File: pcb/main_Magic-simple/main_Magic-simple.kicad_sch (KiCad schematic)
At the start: 57 parts, among them J1 XT30PW-M, J10 ESC1, J11 ESC2, J12 ESC3, J15 ESC_VM, J2 MPU6050, J4 Encoder1, J5 Encoder2, J9 Sensors, Q1 IRLML2502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

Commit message: pcbAAAAA
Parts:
- removed C10, C9: 10nF, Capacitor_SMD:C_0805_2012Metric, symbol Device:C_Small
- removed C26: 100nF, Capacitor_SMD:C_0805_2012Metric, symbol Device:C_Small
- removed C6: 100nF, Capacitor_SMD:C_0603_1608Metric, symbol Device:C_Small
- removed D2: LED_On, MixLib:LED_0805_2012Metric, symbol Device:LED_Small
- removed D5: WS2812B, LED_SMD:LED_WS2812B_PLCC4_5.0x5.0mm_P3.2mm, symbol LED:WS2812B
- removed J1: XT30PW-M, XT30PW-M:AMASS_XT30PW-M, symbol MixLib:XT30PW-M
- removed J15: ESC_VM, TerminalBlock_Phoenix:TerminalBlock_Phoenix_PT-1,5-6-3.5-H_1x06_P3.50mm_Horizontal, symbol Connector:Screw_Terminal_01x06
- removed J4: Encoder1, Connector_JST:JST_XH_B3B-XH-A_1x03_P2.50mm_Vertical, symbol Connector:Conn_01x03_Pin
- removed J5: Encoder2, Connector_JST:JST_XH_B3B-XH-A_1x03_P2.50mm_Vertical, symbol Connector:Conn_01x03_Pin
- removed JP1: Jumper_2_Small_Open, Resistor_SMD:R_1206_3216Metric, symbol Jumper:Jumper_2_Small_Open
- removed R1: 1k, Resistor_SMD:R_0603_1608Metric, symbol Device:R_Small
- removed R7: 100, Resistor_SMD:R_0805_2012Metric, symbol Device:R_Small
- removed SW3: Boot_SW, MixLib:SW_Slide-03_P2.54_L9_W4_H7, symbol Switch:SW_SPST
- removed U2: ACS712-30A, Package_SO:SOIC-8_3.9x4.9mm_P1.27mm, symbol Sensor_Current:ACS712xLCTR-20A
- removed U3: ACS712-20A, Package_SO:SOIC-8_3.9x4.9mm_P1.27mm, symbol Sensor_Current:ACS712xLCTR-20A
- added C1: 100nF, Capacitor_SMD:C_0805_2012Metric, symbol Device:C_Small
- added D6: LED_BLUE, MixLib:LED_0805_2012Metric, symbol Device:LED_Small
- added F2: 1100mAh, Fuse:Fuse_1812_4532Metric_Pad1.30x3.40mm_HandSolder, symbol Device:Polyfuse
- added J1: PW, Connector_JST:JST_XH_S2B-XH-A_1x02_P2.50mm_Horizontal, symbol Connector:Conn_01x02_Pin
- added J14: UART_Out, Connector_JST:JST_XH_S4B-XH-A_1x04_P2.50mm_Horizontal, symbol Connector:Conn_01x04_Pin
- added J3: LiPo-Battery, TerminalBlock_Phoenix:TerminalBlock_Phoenix_PT-1,5-2-3.5-H_1x02_P3.50mm_Horizontal, symbol Connector:Screw_Terminal_01x02
- added R10: 330, Resistor_SMD:R_0805_2012Metric, symbol Device:R_Small
- added SW3: Boot_Push, Button_Switch_SMD:SW_SPST_CK_RS282G05A3, symbol Switch:SW_Push
- added TP1: Curr1, symbol Connector:TestPoint
- added TP2: Curr2, symbol Connector:TestPoint
- added TP3: Enc1, symbol Connector:TestPoint
- added TP4: Enc2, symbol Connector:TestPoint
- added U6: Mini360, MixLib:Mini360_step-down, symbol MixLib:Mini360
- C11: value 10uF -> 47uF; footprint Capacitor_SMD:C_0805_2012Metric -> Capacitor_SMD:CP_Elec_6.3x5.4
- C28: value 100uF -> 470uF; footprint Capacitor_SMD:CP_Elec_6.3x5.4 -> (none)
- C3: value 1uF -> 22uF
- C5: footprint Capacitor_SMD:C_0603_1608Metric -> Capacitor_SMD:C_0805_2012Metric
- C7: value 100nF -> 1uF
- F1: value 300mA -> 500mA
- R4: value 330 -> 20
- R5: value 100 -> 330
- R6: value 10k -> 1k; footprint Resistor_SMD:R_0805_2012Metric -> Resistor_SMD:R_0603_1608Metric
- R8: value 330 -> 10k
- SW1: footprint MixLib:SW_Slide-03_P2.54_L9_W4_H7 -> (none)
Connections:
- net LEDs is gone; now on net LED_RGB: D3.4 (DIN)
- net +3.3V: now also C5.1, C1.1, F2.2, J1.2 (Pin_2), J14.4 (Pin_4); no longer C11.1, C12.1, C5.2, J9.9 (Pin_9)
- net BOOT: now also SW3.1
- net BUZ: now also R10.1; no longer R8.2
- net CurrESC1&2: now also TP1.1; no longer U1.13 (IO14)
- net CurrESC2: now also TP2.1; no longer U1.12 (IO27)
- net Data_EN: no longer R6.2
- net Enc1: now also TP3.1; no longer U1.11 (IO26)
- net Enc2: now also TP4.1; no longer U1.10 (IO25)
- net GND: now also C5.2, R6.2, R8.1, C1.2, J1.1 (Pin_1), J14.3 (Pin_3), J3.1 (Pin_1), SW3.2, U6.2 (GND); no longer C5.1, R6.1
- net RX: now also J14.1 (Pin_1)
- net TX: now also J14.2 (Pin_2)
- net VM: now also D1.2 (A), J3.2 (Pin_2); no longer SW1.1 (A)
- net Vb: now also SW1.1 (A)
- net at Q1.1 (G): now also R8.2, R10.2; no longer R8.1
- net LED_BLUE: now reaches U1.24 (IO2)
- net LED_BLUE: now also D6.2 (A)
- net LED_RGB: now reaches U1.29 (IO5)
- net at SW1.2 (B): now also U6.1 (IN); no longer D1.2 (A)
- new net: C11.1, C12.1, J9.9 (Pin_9)
- new net: D6.1 (K), R6.1
- new net: F2.1, U6.3 (OUT)
- no-connect marks 5 -> 4
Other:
- removed sheet CH340C
- removed sheet StepDown_CN3903
- note added: "RGB LED"
- note removed: "Bidirectionals"
- note removed: "ESC Current Sensors"
- note removed: "ESP32 connections"
- note removed: "Inputs"
- note removed: "Outputs"
- note removed: "RGB LEDs"
- note removed: "X"
- moved on the sheet: BZ1, C11, C12, C2, C24, C28, D1, D3, H1, H10, H2, H3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

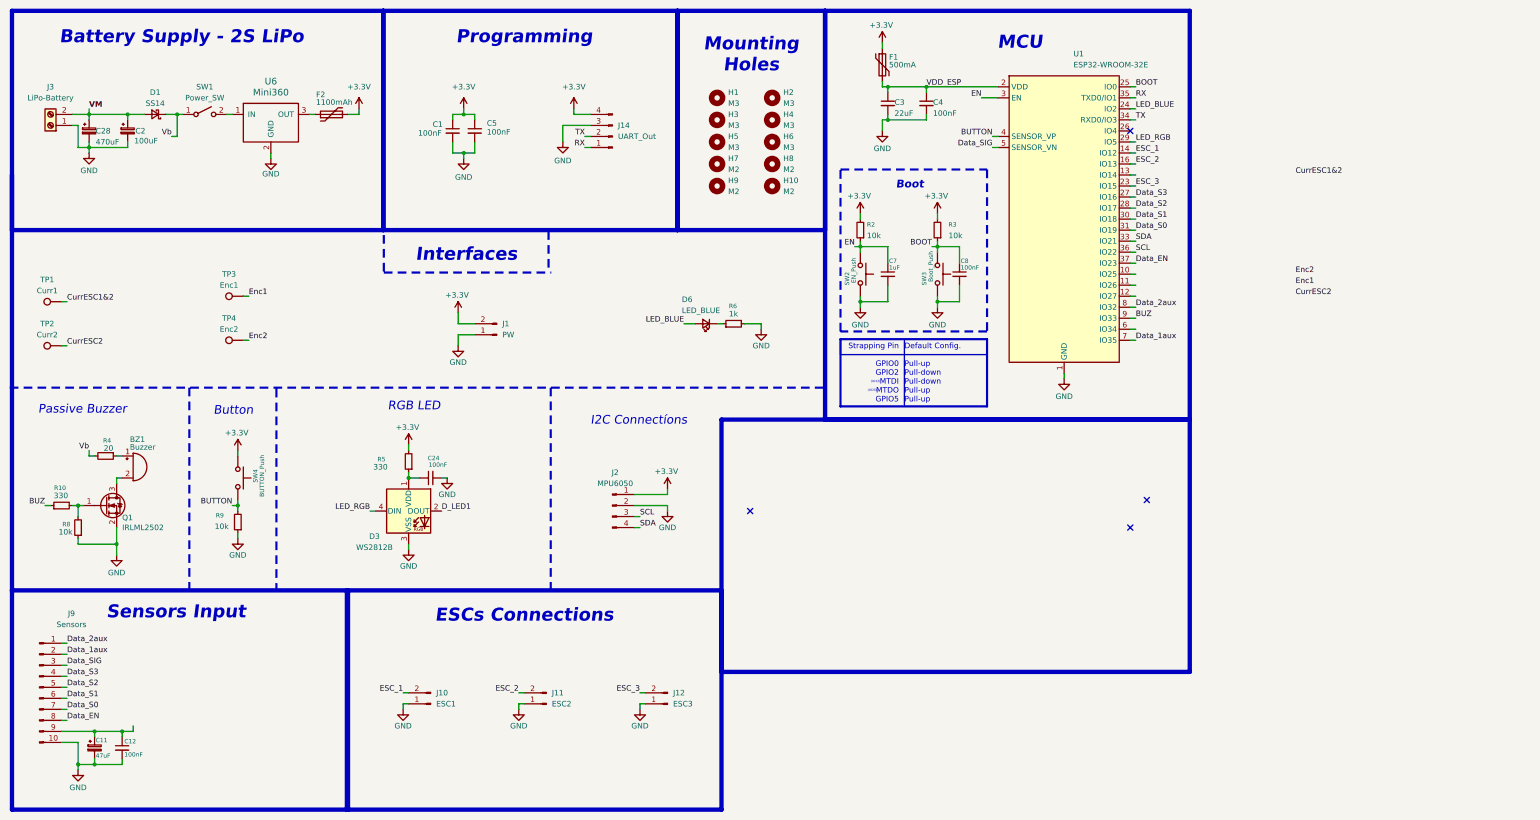
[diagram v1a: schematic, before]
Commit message: simple main board added and donde
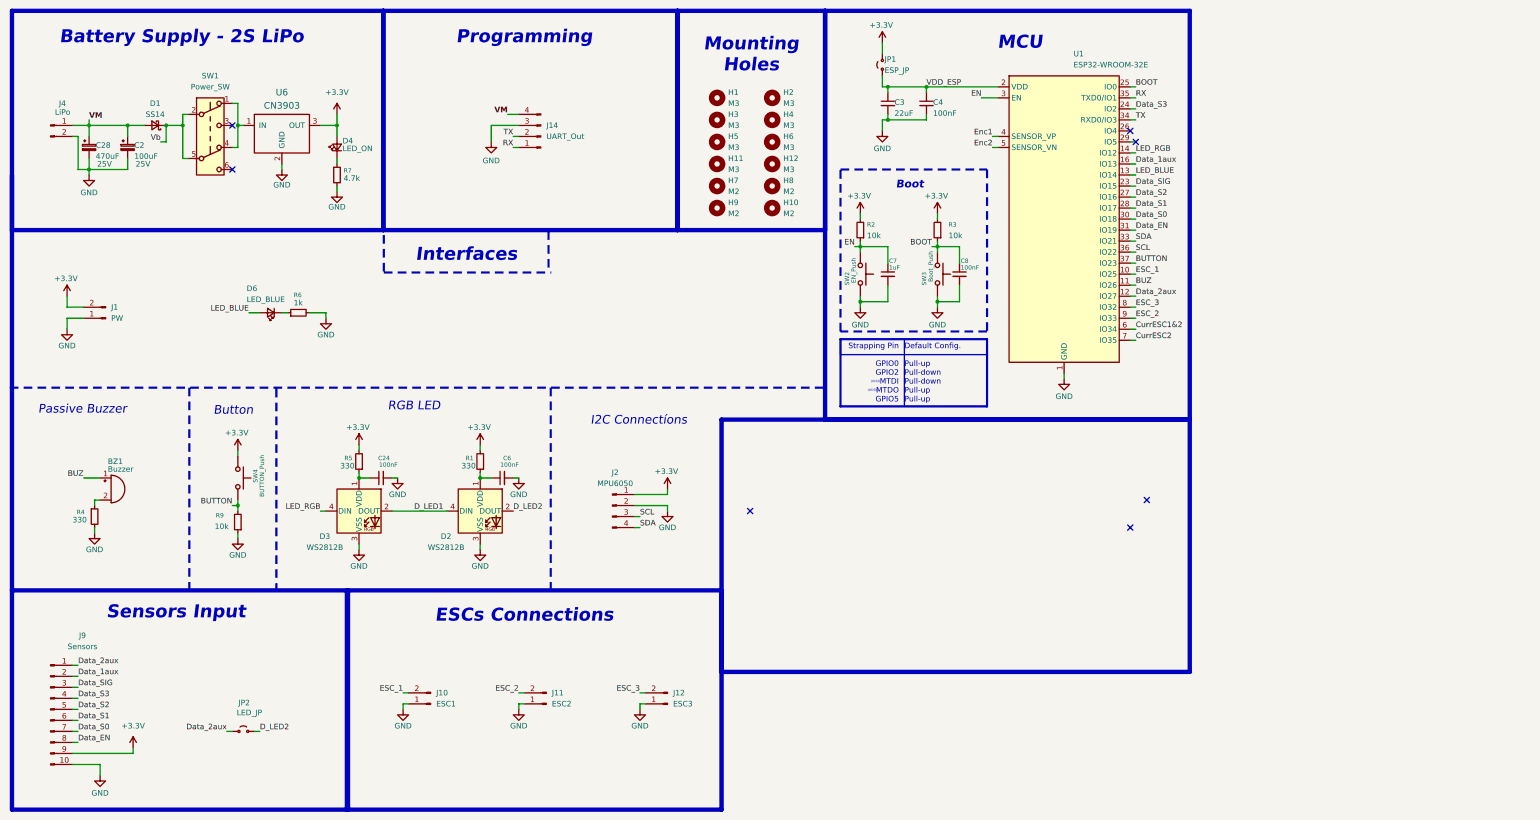
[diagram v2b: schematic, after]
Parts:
- removed C1, C12, C5: 100nF, Capacitor_SMD:C_0805_2012Metric, symbol Device:C_Small
- removed C11: 47uF, Capacitor_SMD:CP_Elec_6.3x5.4, symbol Device:C_Polarized_Small
- removed F1: 500mA, Fuse:Fuse_1812_4532Metric_Pad1.30x3.40mm_HandSolder, symbol Device:Polyfuse
- removed F2: 1100mAh, Fuse:Fuse_1812_4532Metric_Pad1.30x3.40mm_HandSolder, symbol Device:Polyfuse
- removed J3: LiPo-Battery, TerminalBlock_Phoenix:TerminalBlock_Phoenix_PT-1,5-2-3.5-H_1x02_P3.50mm_Horizontal, symbol Connector:Screw_Terminal_01x02
- removed Q1: IRLML2502, Package_TO_SOT_SMD:SOT-23, symbol Transistor_FET:IRLML2060
- removed R10: 330, Resistor_SMD:R_0805_2012Metric, symbol Device:R_Small
- removed R8: 10k, Resistor_SMD:R_0805_2012Metric, symbol Device:R_Small
- removed SW1: Power_SW, symbol Switch:SW_SPST
- removed TP1: Curr1, symbol Connector:TestPoint
- removed TP2: Curr2, symbol Connector:TestPoint
- removed TP3: Enc1, symbol Connector:TestPoint
- removed TP4: Enc2, symbol Connector:TestPoint
- added C6: 100nF, Capacitor_SMD:C_0805_2012Metric, symbol Device:C_Small
- added D2: WS2812B, LED_SMD:LED_WS2812B_PLCC4_5.0x5.0mm_P3.2mm, symbol LED:WS2812B
- added D4: LED_ON, MixLib:LED_0805_2012Metric, symbol Device:LED_Small
- added H11, H12: M3, MountingHole:MountingHole_3mm, symbol Mechanical:MountingHole
- added J4: LiPo, Connector_JST:JST_XH_S2B-XH-A_1x02_P2.50mm_Horizontal, symbol Connector:Conn_01x02_Pin
- added JP1: ESP_JP, Resistor_SMD:R_1206_3216Metric, symbol Jumper:Jumper_2_Small_Open
- added JP2: LED_JP, Resistor_SMD:R_1206_3216Metric, symbol Jumper:Jumper_2_Small_Open
- added R1: 330, Resistor_SMD:R_0805_2012Metric, symbol Device:R_Small
- added R7: 4.7k, Resistor_SMD:R_0603_1608Metric, symbol Device:R_Small
- added SW1: Power_SW, Button_Switch_THT:SW_Push_2P2T_Toggle_CK_PVA2OAH5xxxxxxV2, symbol Switch:SW_Push_DPDT
- C2: footprint Capacitor_SMD:CP_Elec_6.3x5.4 -> Capacitor_THT:CP_Radial_D8.0mm_P3.50mm; Max Tension (none) -> 25V
- C28: footprint (none) -> Capacitor_THT:CP_Radial_D8.0mm_P3.50mm; Max Tension (none) -> 25V
- J1: footprint Connector_JST:JST_XH_S2B-XH-A_1x02_P2.50mm_Horizontal -> Connector_JST:JST_XH_B2B-XH-A_1x02_P2.50mm_Vertical
- R4: value 20 -> 330; footprint Resistor_SMD:R_1206_3216Metric -> Resistor_SMD:R_0805_2012Metric
- SW2, SW3: footprint Button_Switch_SMD:SW_SPST_CK_RS282G05A3 -> MixLib:SW_Push_SPST_NO_Alps_SKRK_Handsolder
- U6: value Mini360 -> CN3903
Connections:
- net +3.3V: now also J9.9 (Pin_9), U6.3 (OUT), D4.2 (A), JP1.2 (B), R1.2; no longer J14.4 (Pin_4)
- net BUTTON: now also U1.37 (IO23); no longer U1.4 (SENSOR_VP)
- net BUZ: now also BZ1.1 (+), U1.11 (IO26); no longer U1.9 (IO33)
- net CurrESC1&2: now also U1.6 (IO34)
- net CurrESC2: now also U1.7 (IO35)
- net D_LED1: now also D2.4 (DIN)
- net Data_1aux: now also U1.16 (IO13); no longer U1.7 (IO35)
- net Data_2aux: now also U1.12 (IO27), JP2.1 (A); no longer U1.8 (IO32)
- net Data_EN: now also U1.31 (IO19); no longer U1.37 (IO23)
- net Data_S0: now also U1.30 (IO18); no longer U1.31 (IO19)
- net Data_S1: now also U1.28 (IO17); no longer U1.30 (IO18)
- net Data_S2: now also U1.27 (IO16); no longer U1.28 (IO17)
- net Data_S3: now also U1.24 (IO2); no longer U1.27 (IO16)
- net Data_SIG: now also U1.23 (IO15); no longer U1.5 (SENSOR_VN)
- net ESC_1: now also U1.10 (IO25); no longer U1.14 (IO12)
- net ESC_2: now also U1.9 (IO33); no longer U1.16 (IO13)
- net ESC_3: now also U1.8 (IO32); no longer U1.23 (IO15)
- net Enc1: now also U1.4 (SENSOR_VP)
- net Enc2: now also U1.5 (SENSOR_VN)
- net GND: now also R4.2, C6.2, D2.3 (VSS), J4.2 (Pin_2), R7.2
- net LED_BLUE: now also U1.13 (IO14); no longer U1.24 (IO2)
- net LED_RGB: now also U1.14 (IO12); no longer U1.29 (IO5)
- net VDD_ESP: now also JP1.1 (A)
- net VM: now also J14.4 (Pin_4), J4.1 (Pin_1)
- net Vb: now also SW1.2 (B), SW1.5 (B); no longer R4.2
- net at R4.1: now also BZ1.2 (-); no longer BZ1.1 (+)
- net at U6.1 (IN): now also SW1.1 (A), SW1.4 (A)
- new net: C6.1, D2.1 (VDD), R1.1
- new net: D4.1 (K), R7.1
- new net D_LED2: D2.2 (DOUT), JP2.2 (B)
- no-connect marks 4 -> 7
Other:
- moved on the sheet: BZ1, C24, C28, D1, D3, D6, H10, H7, H8, H9, J1, J14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
